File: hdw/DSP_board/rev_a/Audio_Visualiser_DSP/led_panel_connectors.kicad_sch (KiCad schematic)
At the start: 18 parts

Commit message: add simulation data for speaker input path
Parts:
- gave numbers to parts that had none: 5
- renumbered D601 to D2101

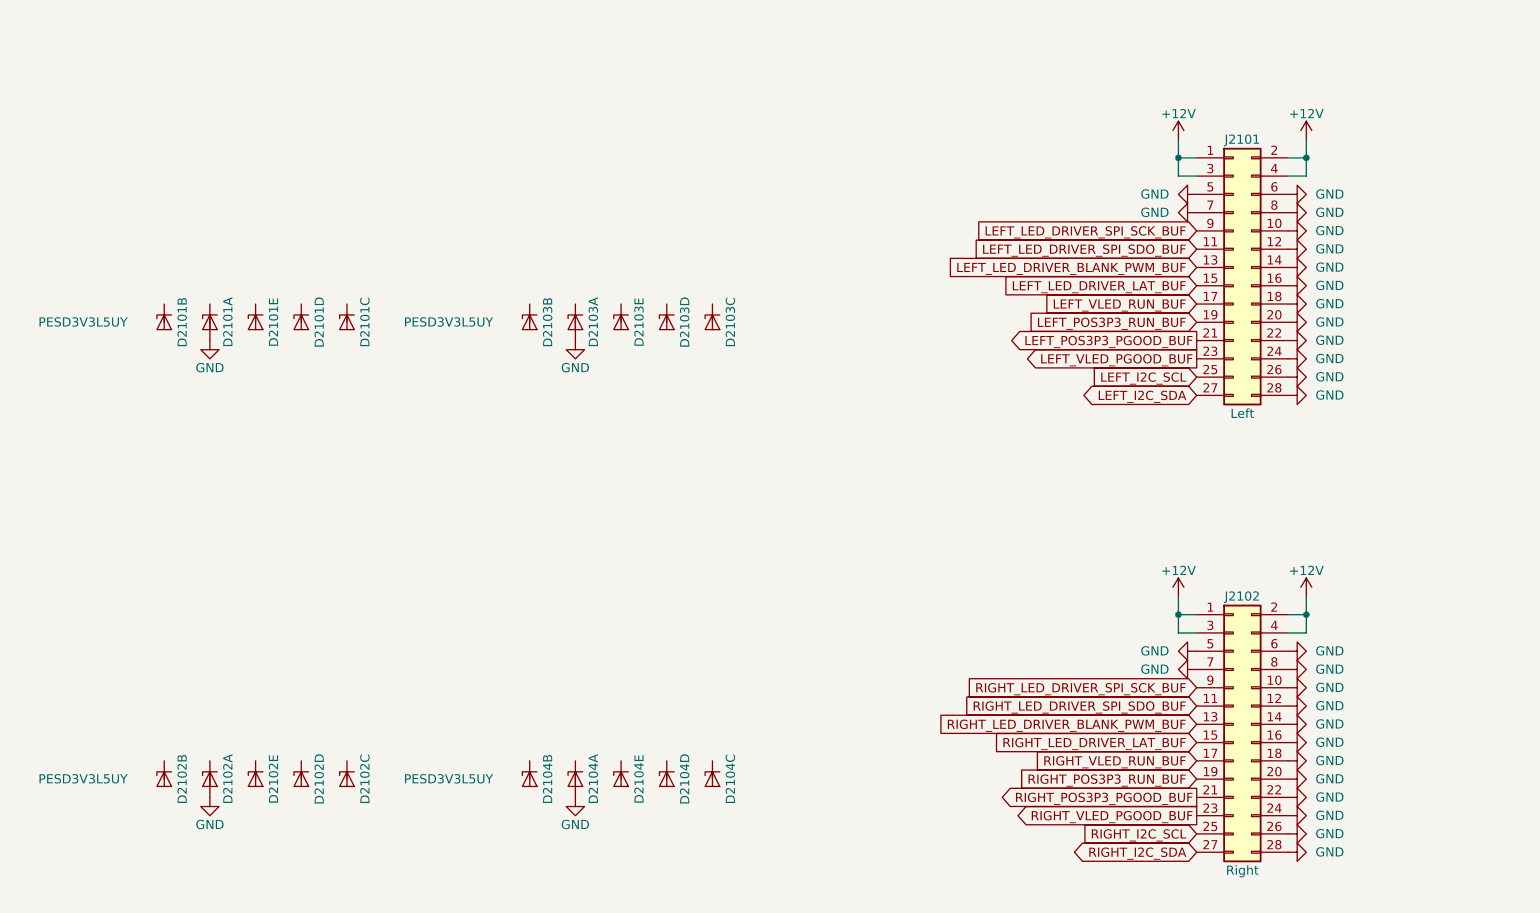
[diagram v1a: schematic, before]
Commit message: Added a bunch of stuff to the schematic
Moved to adafruit I2C rotary encoder module. Added signal test points. Added some design schematic notes. Added LEd output connector ESD diodes. Consolidated on a single schottky diode. Connected most signals to MCU
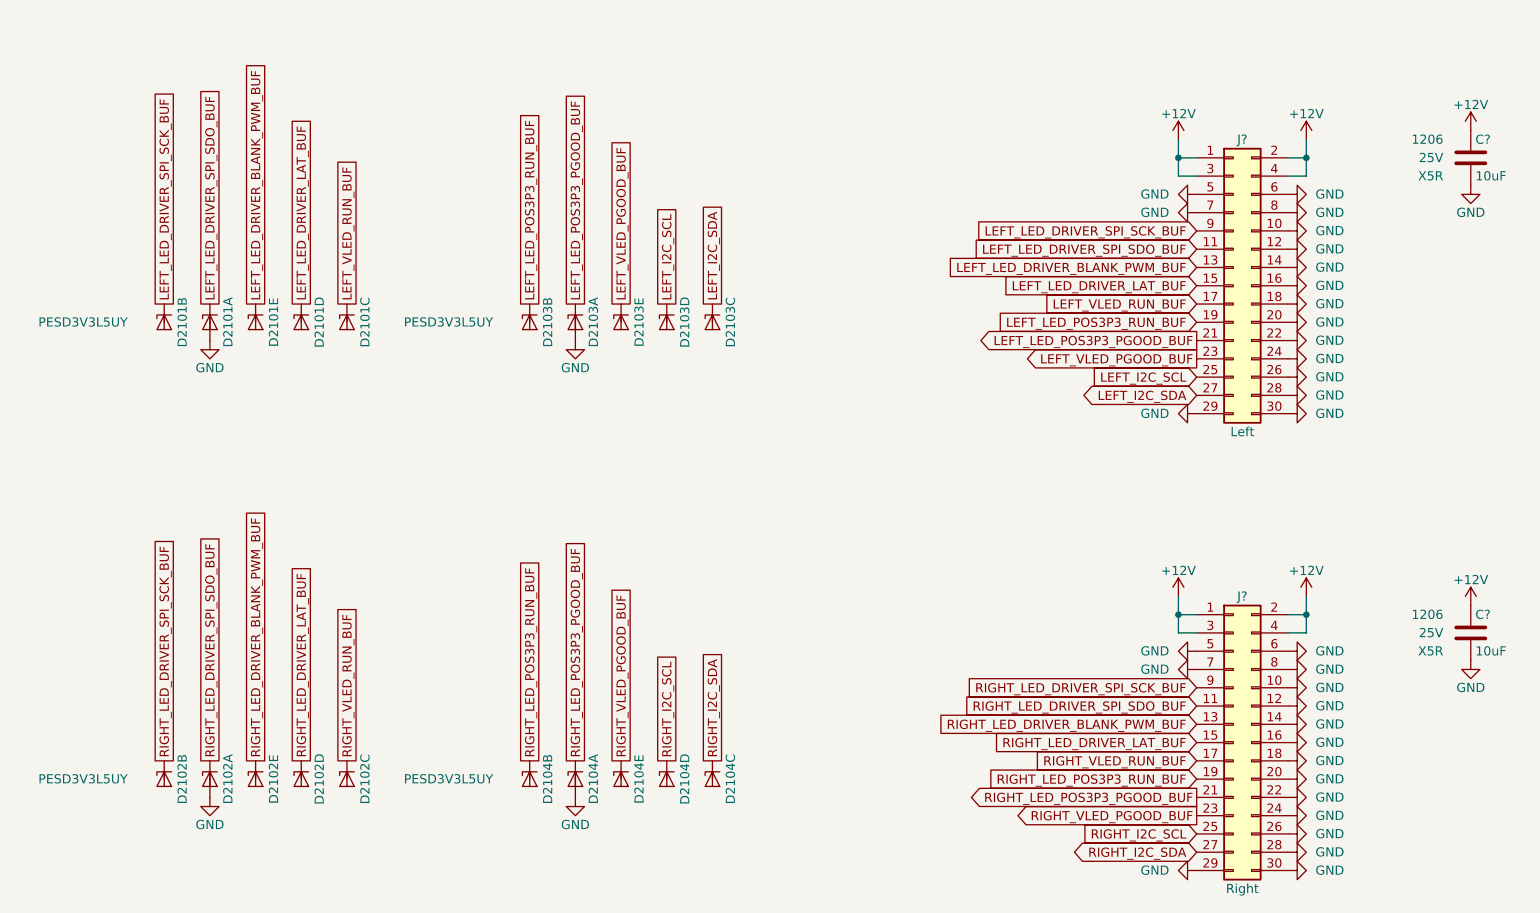
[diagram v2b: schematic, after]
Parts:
- removed J2101: Left, symbol Connector_Generic:Conn_02x14_Odd_Even
- removed J2102: Right, symbol Connector_Generic:Conn_02x14_Odd_Even
- added C? (x2): 10uF, Capacitors_SMD:C_1206, symbol Custom_Library:C_Custom
- added J?: Right, Connector_IDC:IDC-Header_2x15_P2.54mm_Vertical, symbol Connector_Generic:Conn_02x15_Odd_Even
- added J?: Left, Connector_IDC:IDC-Header_2x15_P2.54mm_Vertical, symbol Connector_Generic:Conn_02x15_Odd_Even
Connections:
- net +12V: now also C?.1, C?.1, J?.1 (Pin_1), J?.1 (Pin_1), J?.2 (Pin_2), J?.2 (Pin_2), J?.3 (Pin_3), J?.3 (Pin_3), J?.4 (Pin_4), J?.4 (Pin_4)
- net GND: now also C?.2, C?.2, J?.10 (Pin_10), J?.10 (Pin_10), J?.12 (Pin_12), J?.12 (Pin_12), J?.14 (Pin_14), J?.14 (Pin_14), J?.16 (Pin_16), J?.16 (Pin_16), J?.18 (Pin_18), J?.18 (Pin_18), J?.20 (Pin_20), J?.20 (Pin_20), J?.22 (Pin_22), J?.22 (Pin_22), J?.24 (Pin_24), J?.24 (Pin_24), J?.26 (Pin_26), J?.26 (Pin_26), J?.28 (Pin_28), J?.28 (Pin_28), J?.29 (Pin_29), J?.29 (Pin_29), J?.30 (Pin_30), J?.30 (Pin_30), J?.5 (Pin_5), J?.5 (Pin_5), J?.6 (Pin_6), J?.6 (Pin_6), J?.7 (Pin_7), J?.7 (Pin_7), J?.8 (Pin_8), J?.8 (Pin_8)
- net LEFT_I2C_SCL: now also D2103.5 (K4), J?.25 (Pin_25)
- net LEFT_I2C_SDA: now also D2103.4 (K3), J?.27 (Pin_27)
- net LEFT_LED_DRIVER_BLANK_PWM_BUF: now also D2101.6 (K5), J?.13 (Pin_13)
- net LEFT_LED_DRIVER_LAT_BUF: now also D2101.5 (K4), J?.15 (Pin_15)
- net LEFT_LED_DRIVER_SPI_SCK_BUF: now also D2101.3 (K2), J?.9 (Pin_9)
- net LEFT_LED_DRIVER_SPI_SDO_BUF: now also D2101.1 (K1), J?.11 (Pin_11)
- net LEFT_VLED_PGOOD_BUF: now also D2103.6 (K5), J?.23 (Pin_23)
- net LEFT_VLED_RUN_BUF: now also D2101.4 (K3), J?.17 (Pin_17)
- net RIGHT_I2C_SCL: now also D2104.5 (K4), J?.25 (Pin_25)
- net RIGHT_I2C_SDA: now also D2104.4 (K3), J?.27 (Pin_27)
- net RIGHT_LED_DRIVER_BLANK_PWM_BUF: now also D2102.6 (K5), J?.13 (Pin_13)
- net RIGHT_LED_DRIVER_LAT_BUF: now also D2102.5 (K4), J?.15 (Pin_15)
- net RIGHT_LED_DRIVER_SPI_SCK_BUF: now also D2102.3 (K2), J?.9 (Pin_9)
- net RIGHT_LED_DRIVER_SPI_SDO_BUF: now also D2102.1 (K1), J?.11 (Pin_11)
- net RIGHT_VLED_PGOOD_BUF: now also D2104.6 (K5), J?.23 (Pin_23)
- net RIGHT_VLED_RUN_BUF: now also D2102.4 (K3), J?.17 (Pin_17)
- net LEFT_LED_POS3P3_PGOOD_BUF: now reaches D2103.1 (K1)
- net LEFT_LED_POS3P3_PGOOD_BUF: now also J?.21 (Pin_21)
- net LEFT_LED_POS3P3_RUN_BUF: now reaches D2103.3 (K2)
- net LEFT_LED_POS3P3_RUN_BUF: now also J?.19 (Pin_19)
- net RIGHT_LED_POS3P3_RUN_BUF: now reaches D2104.3 (K2)
- net RIGHT_LED_POS3P3_RUN_BUF: now also J?.19 (Pin_19)
- net RIGHT_LED_POS3P3_PGOOD_BUF: now reaches D2104.1 (K1)
- net RIGHT_LED_POS3P3_PGOOD_BUF: now also J?.21 (Pin_21)

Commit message: Added simulation outputs, sim readme
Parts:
- gave numbers to parts that had none: 4

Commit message: add new digikey pns
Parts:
- C2101, C2102: Digi-Key PN 1276-1075-1-ND -> 445-6862-1-ND
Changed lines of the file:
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@@
 			)
 		)
-		(property "Digi-Key PN" "1276-1075-1-ND"
+		(property "Digi-Key PN" "445-6862-1-ND"
 			(at 234.315 30.48 0)
 			(hide yes)
@@
 			)
 		)
-		(property "Digi-Key PN" "1276-1075-1-ND"
+		(property "Digi-Key PN" "445-6862-1-ND"
 			(at 234.315 96.52 0)
 			(hide yes)

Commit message: fix a lot of digikey pns which are out of stock, find alternate inductors, change I2C buffers
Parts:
- D2101, D2102, D2103, D2104: value PESD3V3L5UY -> PESD5V0L5UYF; Digi-Key PN 1727-3828-1-ND -> 1727-PESD5V0L5UYFCT-ND
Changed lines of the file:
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@@
 			)
 		)
-		(property "Value" "PESD3V3L5UY"
+		(property "Value" "PESD5V0L5UYF"
 			(at 58.42 66.04 0)
 			(hide yes)
@@
 			)
 		)
-		(property "Digi-Key PN" "1727-3828-1-ND"
+		(property "Digi-Key PN" "1727-PESD5V0L5UYFCT-ND"
 			(at 60.96 66.04 0)
 			(hide yes)
@@
 			)
 		)
-		(property "Value" "PESD3V3L5UY"
+		(property "Value" "PESD5V0L5UYF"
 			(at 87.63 66.04 90)
 			(show_name no)
@@
 			)
 		)
-		(property "Digi-Key PN" "1727-3828-1-ND"
+		(property "Digi-Key PN" "1727-PESD5V0L5UYFCT-ND"
 			(at 99.06 66.04 0)
 			(hide yes)
@@
 			)
 		)
-		(property "Value" "PESD3V3L5UY"
+		(property "Value" "PESD5V0L5UYF"
 			(at 39.37 129.54 0)
 			(hide yes)
@@
 			)
 		)
-		(property "Digi-Key PN" "1727-3828-1-ND"
+		(property "Digi-Key PN" "1727-PESD5V0L5UYFCT-ND"
 			(at 41.91 129.54 0)
 			(hide yes)
@@
 			)
 		)
-		(property "Value" "PESD3V3L5UY"
+		(property "Value" "PESD5V0L5UYF"
 			(at 39.37 66.04 0)
 			(hide yes)
@@
 			)
 		)
-		(property "Digi-Key PN" "1727-3828-1-ND"
+		(property "Digi-Key PN" "1727-PESD5V0L5UYFCT-ND"
 			(at 41.91 66.04 0)
 			(hide yes)
@@
 			)
 		)
-		(property "Value" "PESD3V3L5UY"
+		(property "Value" "PESD5V0L5UYF"
 			(at 64.77 66.04 0)
 			(hide yes)
@@
 			)
 		)
-		(property "Digi-Key PN" "1727-3828-1-ND"
+		(property "Digi-Key PN" "1727-PESD5V0L5UYFCT-ND"
 			(at 67.31 66.04 0)
 			(hide yes)
@@
 			)
 		)
-		(property "Value" "PESD3V3L5UY"
+		(property "Value" "PESD5V0L5UYF"
 			(at 64.77 129.54 0)
 			(hide yes)
@@
 			)
 		)
-		(property "Digi-Key PN" "1727-3828-1-ND"
+		(property "Digi-Key PN" "1727-PESD5V0L5UYFCT-ND"
 			(at 67.31 129.54 0)
 			(hide yes)
@@
 			)
 		)
-		(property "Value" "PESD3V3L5UY"
+		(property "Value" "PESD5V0L5UYF"
 			(at 115.57 129.54 0)
 			(hide yes)
@@
 			)
 		)
-		(property "Digi-Key PN" "1727-3828-1-ND"
+		(property "Digi-Key PN" "1727-PESD5V0L5UYFCT-ND"
 			(at 118.11 129.54 0)
 			(hide yes)
@@
 			)
 		)
-		(property "Value" "PESD3V3L5UY"
+		(property "Value" "PESD5V0L5UYF"
 			(at 52.07 66.04 0)
 			(hide yes)
@@
 			)
 		)
-		(property "Digi-Key PN" "1727-3828-1-ND"
+		(property "Digi-Key PN" "1727-PESD5V0L5UYFCT-ND"
 			(at 54.61 66.04 0)
 			(hide yes)
@@
 			)
 		)
-		(property "Value" "PESD3V3L5UY"
+		(property "Value" "PESD5V0L5UYF"
 			(at 109.22 129.54 0)
 			(hide yes)
@@
 			)
 		)
-		(property "Digi-Key PN" "1727-3828-1-ND"
+		(property "Digi-Key PN" "1727-PESD5V0L5UYFCT-ND"
 			(at 111.76 129.54 0)
 			(hide yes)
@@
 			)
 		)
-		(property "Value" "PESD3V3L5UY"
+		(property "Value" "PESD5V0L5UYF"
 			(at 58.42 129.54 0)
 			(hide yes)
@@
 			)
 		)
-		(property "Digi-Key PN" "1727-3828-1-ND"
+		(property "Digi-Key PN" "1727-PESD5V0L5UYFCT-ND"
 			(at 60.96 129.54 0)
 			(hide yes)
@@
 			)
 		)
-		(property "Value" "PESD3V3L5UY"
+		(property "Value" "PESD5V0L5UYF"
 			(at 115.57 66.04 0)
 			(hide yes)
@@
 			)
 		)
-		(property "Digi-Key PN" "1727-3828-1-ND"
+		(property "Digi-Key PN" "1727-PESD5V0L5UYFCT-ND"
 			(at 118.11 66.04 0)
 			(hide yes)
@@
 			)
 		)
-		(property "Value" "PESD3V3L5UY"
+		(property "Value" "PESD5V0L5UYF"
 			(at 90.17 66.04 0)
 			(hide yes)
@@
 			)
 		)
-		(property "Digi-Key PN" "1727-3828-1-ND"
+		(property "Digi-Key PN" "1727-PESD5V0L5UYFCT-ND"
 			(at 92.71 66.04 0)
 			(hide yes)
@@
 			)
 		)
-		(property "Value" "PESD3V3L5UY"
+		(property "Value" "PESD5V0L5UYF"
 			(at 102.87 66.04 0)
 			(hide yes)
@@
 			)
 		)
-		(property "Digi-Key PN" "1727-3828-1-ND"
+		(property "Digi-Key PN" "1727-PESD5V0L5UYFCT-ND"
 			(at 105.41 66.04 0)
 			(hide yes)
@@
 			)
 		)
-		(property "Value" "PESD3V3L5UY"
+		(property "Value" "PESD5V0L5UYF"
 			(at 102.87 129.54 0)
 			(hide yes)
@@
 			)
 		)
-		(property "Digi-Key PN" "1727-3828-1-ND"
+		(property "Digi-Key PN" "1727-PESD5V0L5UYFCT-ND"
 			(at 105.41 129.54 0)
 			(hide yes)
@@
 			)
 		)
-		(property "Value" "PESD3V3L5UY"
+		(property "Value" "PESD5V0L5UYF"
 			(at 36.83 129.54 90)
 			(show_name no)
@@
 			)
 		)
-		(property "Digi-Key PN" "1727-3828-1-ND"
+		(property "Digi-Key PN" "1727-PESD5V0L5UYFCT-ND"
 			(at 48.26 129.54 0)
 			(hide yes)
@@
 			)
 		)
-		(property "Value" "PESD3V3L5UY"
+		(property "Value" "PESD5V0L5UYF"
 			(at 109.22 66.04 0)
 			(hide yes)
@@
 			)
 		)
-		(property "Digi-Key PN" "1727-3828-1-ND"
+		(property "Digi-Key PN" "1727-PESD5V0L5UYFCT-ND"
 			(at 111.76 66.04 0)
 			(hide yes)
@@
 			)
 		)
-		(property "Value" "PESD3V3L5UY"
+		(property "Value" "PESD5V0L5UYF"
 			(at 90.17 129.54 0)
 			(hide yes)
@@
 			)
 		)
-		(property "Digi-Key PN" "1727-3828-1-ND"
+		(property "Digi-Key PN" "1727-PESD5V0L5UYFCT-ND"
 			(at 92.71 129.54 0)
 			(hide yes)
@@
 			)
 		)
-		(property "Value" "PESD3V3L5UY"
+		(property "Value" "PESD5V0L5UYF"
 			(at 36.83 66.04 90)
 			(show_name no)
@@
 			)
 		)
-		(property "Digi-Key PN" "1727-3828-1-ND"
+		(property "Digi-Key PN" "1727-PESD5V0L5UYFCT-ND"
 			(at 48.26 66.04 0)
 			(hide yes)
@@
 			)
 		)
-		(property "Value" "PESD3V3L5UY"
+		(property "Value" "PESD5V0L5UYF"
 			(at 87.63 129.54 90)
 			(show_name no)
@@
 			)
 		)
-		(property "Digi-Key PN" "1727-3828-1-ND"
+		(property "Digi-Key PN" "1727-PESD5V0L5UYFCT-ND"
 			(at 99.06 129.54 0)
 			(hide yes)
@@
 			)
 		)
-		(property "Value" "PESD3V3L5UY"
+		(property "Value" "PESD5V0L5UYF"
 			(at 52.07 129.54 0)
 			(hide yes)
@@
 			)
 		)
-		(property "Digi-Key PN" "1727-3828-1-ND"
+		(property "Digi-Key PN" "1727-PESD5V0L5UYFCT-ND"
 			(at 54.61 129.54 0)
 			(hide yes)

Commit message: Consolidated onto a single project library
This commit combines all schematic symbols, pcb footprints, and 3d models into a single project library for portability. Still have a few 3d models to add yet. It also removes each individual custom component which had been stored in this repo earlier
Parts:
- C2101, C2102: footprint Capacitors_SMD:C_1206 -> project_lib:C_1206; symbol Custom_Library:C_Custom -> project_lib:C_Custom
- D2101, D2102, D2103, D2104: footprint Package_TO_SOT_SMD:SOT-363_SC-70-6 -> project_lib:SOT-363_SC-70-6; symbol Power_Protection:PESD3V3L5UY -> project_lib:PESD3V3L5UY
- J2101, J2102: footprint Connector_IDC:IDC-Header_2x15_P2.54mm_Vertical -> project_lib:IDC-Header_2x15_P2.54mm_Vertical; symbol Connector_Generic:Conn_02x15_Odd_Even -> project_lib:Conn_02x15_Odd_Even
